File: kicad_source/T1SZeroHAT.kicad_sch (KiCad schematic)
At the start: 44 parts, among them CN1 RASPI-IO, CN2 XY2500R-F-3.81-2P, CN3 SM02B-GHS-TB, CN4 SM02B-GHS-TB, SW1 SS-3235S-L3, U1 LAN8651, Y1 X1E0000210808

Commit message: connected DIOB1 directly to GND as recommended in datasheet
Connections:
- net GND: now also U1.14 (DIOB1)
- no-connect marks 28 -> 27
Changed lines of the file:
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@@
 	)
 	(no_connect
-		(at 68.58 87.63)
-	)
-	(no_connect
 		(at 87.63 182.88)
 	)
@@
 	(wire
 		(pts
+			(xy 66.04 87.63) (xy 66.04 90.17)
+		)
+		(stroke
+			(width 0)
+			(type default)
+		)
+	)
+	(wire
+		(pts
 			(xy 111.76 64.77) (xy 121.92 64.77)
 		)
@@
 		)
 	)
+	(wire
+		(pts
+			(xy 68.58 87.63) (xy 66.04 87.63)
+		)
+		(stroke
+			(width 0)
+			(type default)
+		)
+	)
 	(text "find the full project documentation at https://github.com/generationmake/T1SZeroHAT"
 		(exclude_from_sim no)
@@
 					(unit 1)
 				)
+			)
+		)
+	)
+	(symbol
+		(lib_id "power:GND")
+		(at 66.04 90.17 0)
+		(unit 1)
+		(exclude_from_sim no)
+		(in_bom yes)
+		(on_board yes)
+		(dnp no)
+		(property "Reference" "#PWR015"
+			(at 66.04 96.52 0)
+			(effects
+				(font
+					(size 1.27 1.27)
+				)
+				(hide yes)
+			)
+		)
+		(property "Value" "GND"
+			(at 66.167 94.5642 0)
+			(effects
+				(font
+					(size 1.27 1.27)
+				)
+			)
+		)
+		(property "Footprint" ""
+			(at 66.04 90.17 0)
+			(effects
+				(font
+					(size 1.27 1.27)
+				)
+			)
+		)
+		(property "Datasheet" ""
+			(at 66.04 90.17 0)
+			(effects
+				(font
+					(size 1.27 1.27)
+				)
+			)
+		)
+		(property "Description" ""
+			(at 66.04 90.17 0)
+			(effects
+				(font
+					(size 1.27 1.27)
+				)
+				(hide yes)
+			)
+		)
+		(pin "1"
+		)
+		(instances
+			(project "T1SZeroHAT"
+				(path "/7e630080-3671-4ca2-a703-07968e580250"
+					(reference "#PWR015")
+					(unit 1)
+				)

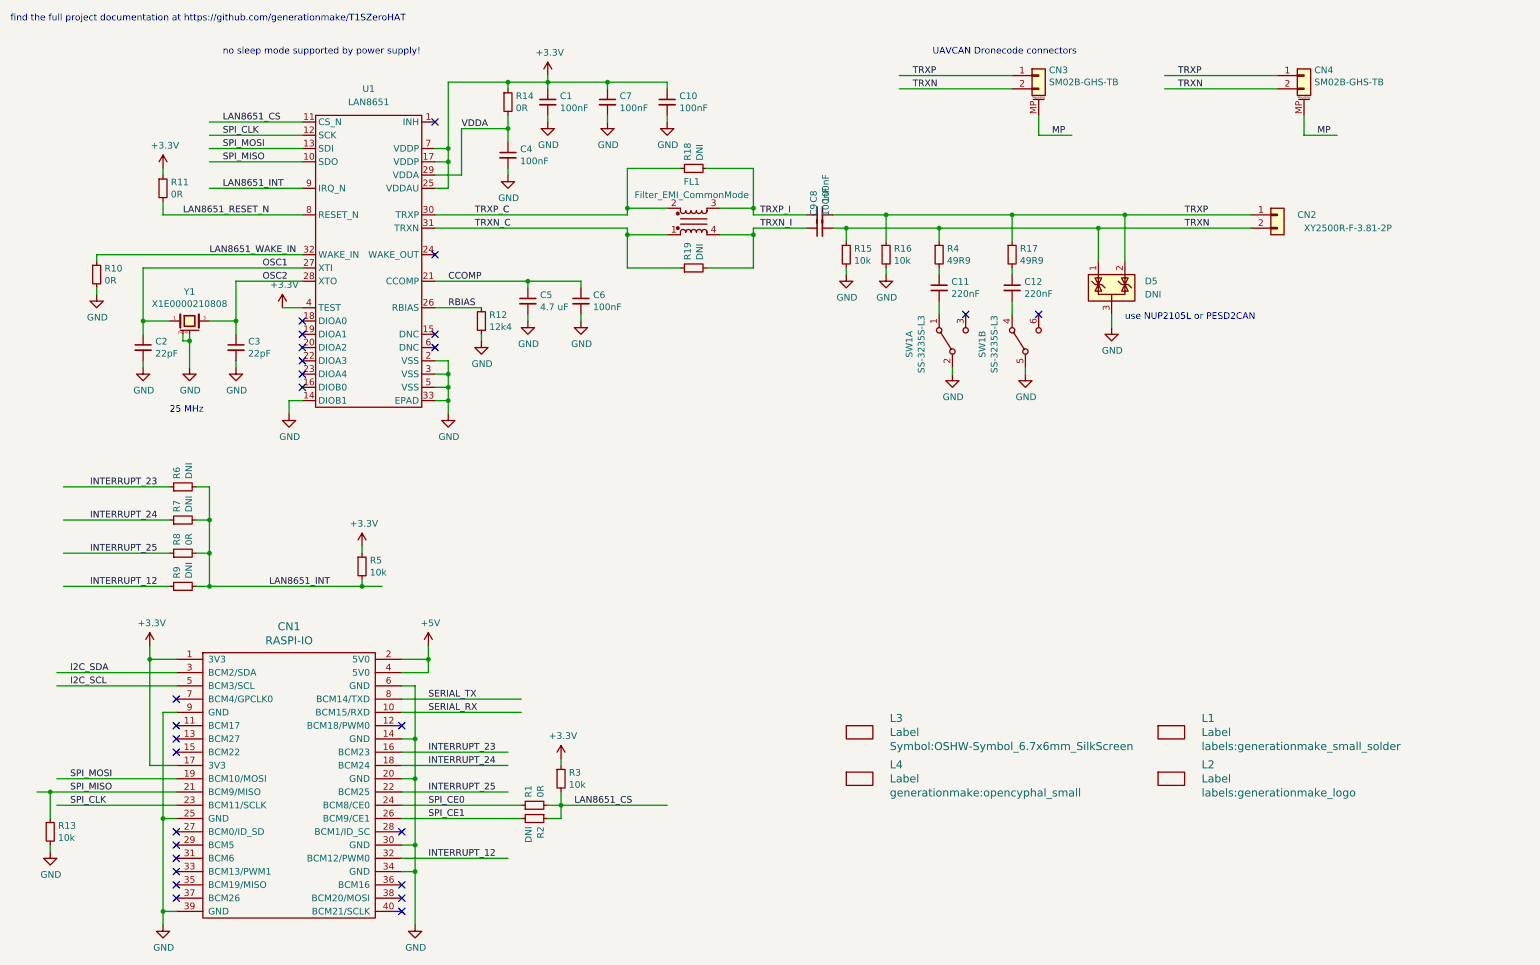
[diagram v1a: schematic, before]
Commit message: reworked power part
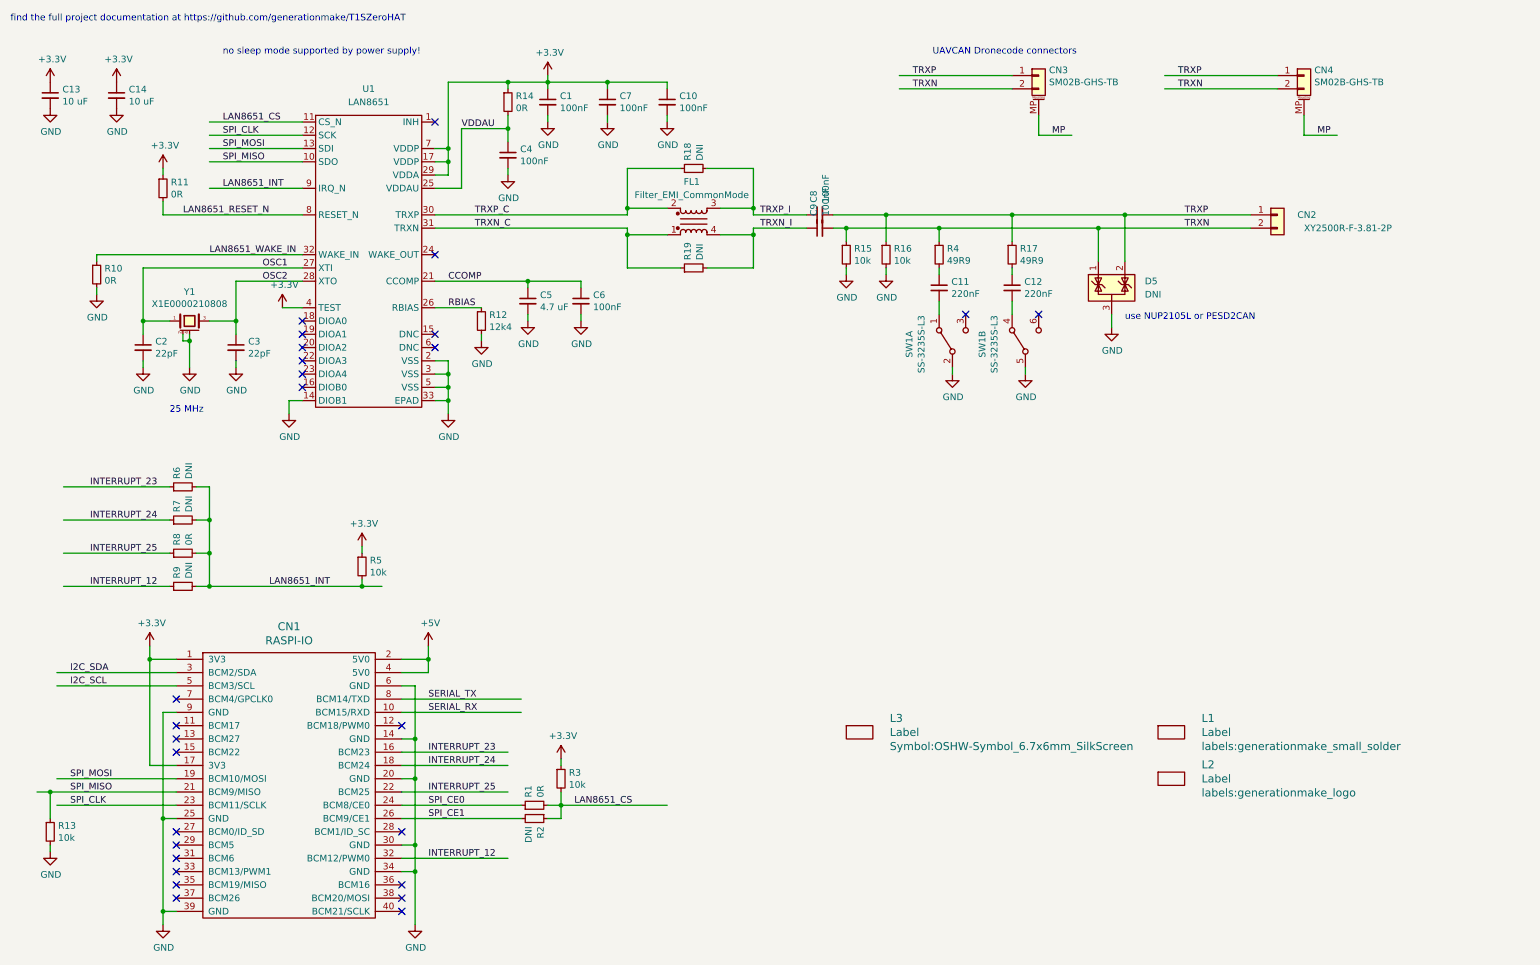
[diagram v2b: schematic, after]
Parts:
- removed L4: Label, generationmake:opencyphal_small, symbol generationmake:Label
- added C13, C14: 10 uF, Capacitor_SMD:C_0603_1608Metric, symbol Device:C_Small
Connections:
- net +3.3V: now also U1.29 (VDDA), C13.1, C14.1; no longer U1.25 (VDDAU)
- net GND: now also C13.2, C14.2
- net VDDA renamed VDDAU
- net VDDAU: now also U1.25 (VDDAU); no longer U1.29 (VDDA)

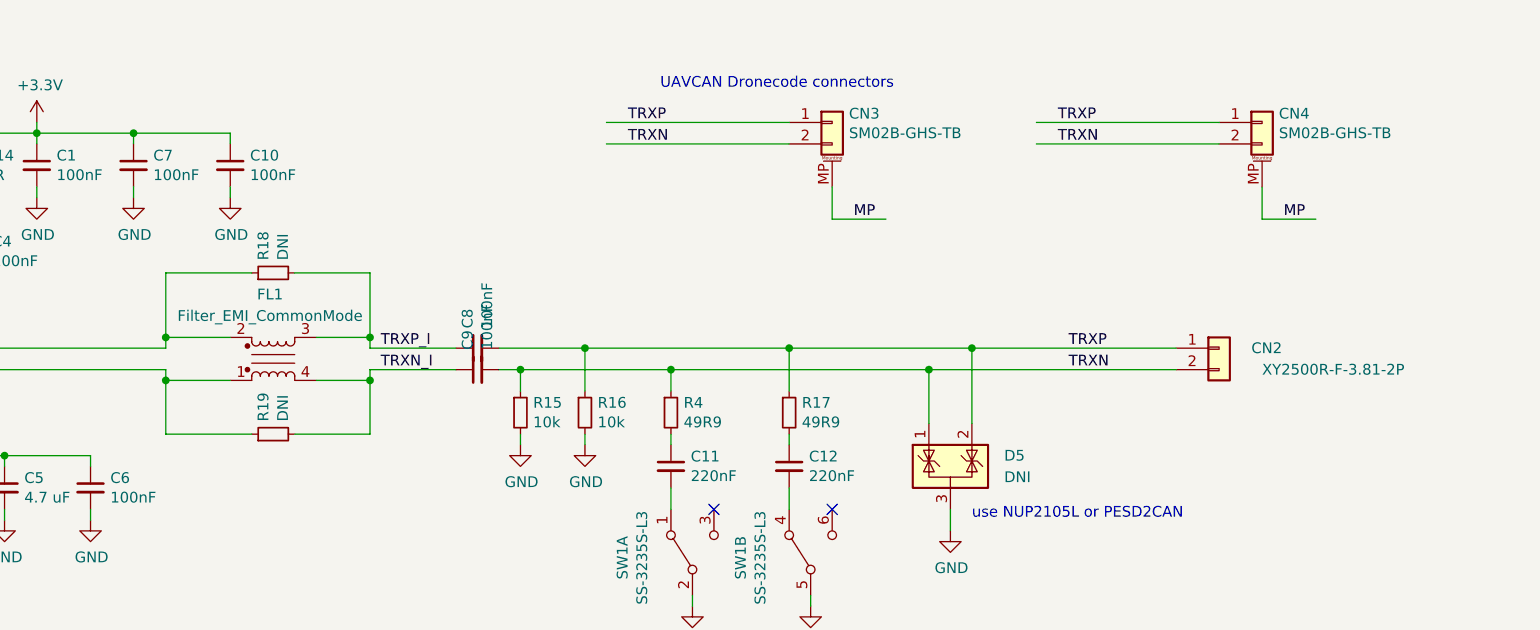
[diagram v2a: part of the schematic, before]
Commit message: corrected common mode choke and added part number
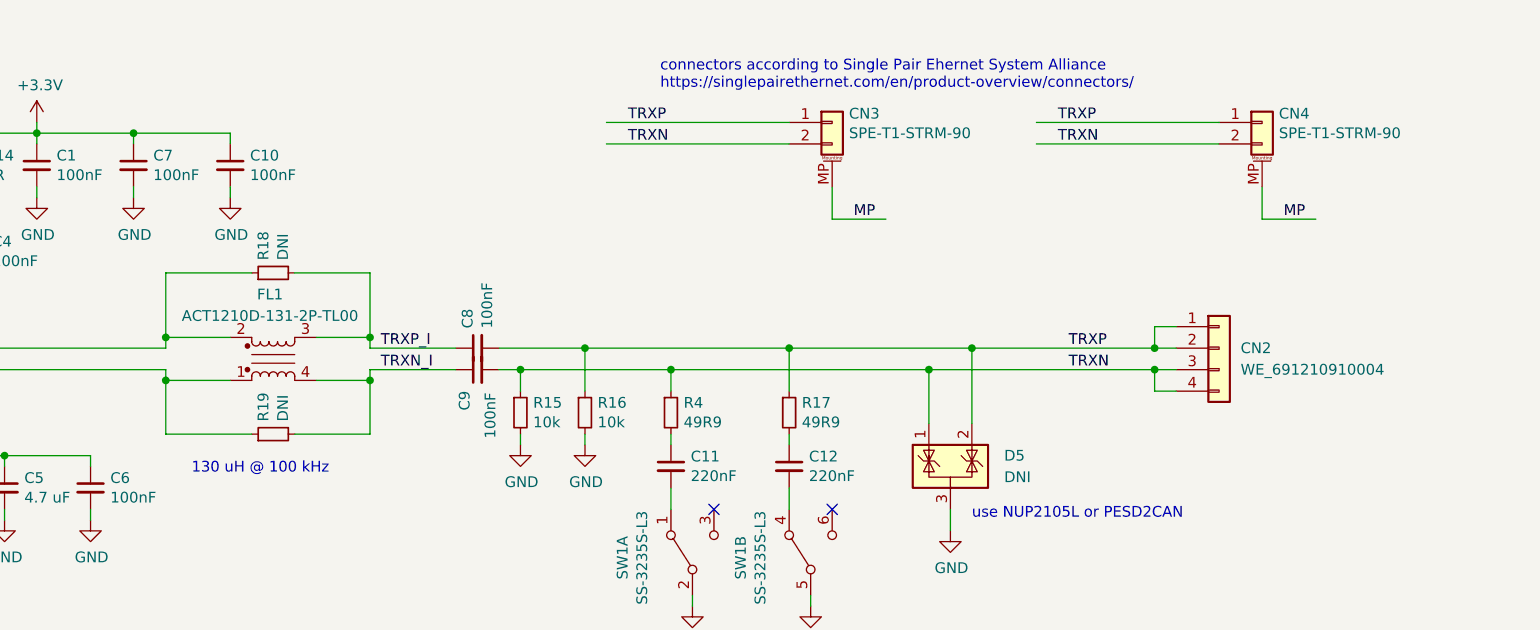
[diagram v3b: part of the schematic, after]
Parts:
- removed CN2: XY2500R-F-3.81-2P, Connector_Phoenix_MC:PhoenixContact_MC_1,5_2-G-3.81_1x02_P3.81mm_Horizontal, symbol Connector_Generic:Conn_01x02
- added CN2: WE_691210910004, generationmake:WE_691210910004, symbol Connector_Generic:Conn_01x04
- CN3, CN4: value SM02B-GHS-TB -> SPE-T1-STRM-90; footprint Connector_JST:JST_GH_SM02B-GHS-TB_1x02-1MP_P1.25mm_Horizontal -> generationmake:SPE-T1-STRM-90
- FL1: value Filter_EMI_CommonMode -> ACT1210D-131-2P-TL00; footprint Filter:Filter_Bourns_SRF0905_6.0x9.2mm -> generationmake:TDK_ACT1210D
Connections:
- net TRXN: now also CN2.3 (Pin_3), CN2.4 (Pin_4)
- net TRXP: now also CN2.1 (Pin_1), CN2.2 (Pin_2)
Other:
- note added: "130 uH @ 100 kHz"
- note added: "connectors according to Single Pair Ehernet System Alliance https://singlepairethernet.com/en/product-overview/connectors/"
- note removed: "UAVCAN Dronecode connectors"
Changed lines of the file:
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@@
 	)
 	(junction
+		(at 247.65 52.07)
+		(diameter 0)
+		(color 0 0 0 0)
+	)
+	(junction
 		(at 127 26.67)
 		(diameter 0)
@@
 	)
 	(junction
+		(at 247.65 54.61)
+		(diameter 0)
+		(color 0 0 0 0)
+	)
+	(junction
 		(at 38.1 72.39)
 		(diameter 0)
@@
 	(wire
 		(pts
+			(xy 247.65 52.07) (xy 250.19 52.07)
+		)
+		(stroke
+			(width 0)
+			(type default)
+		)
+	)
+	(wire
+		(pts
 			(xy 111.76 64.77) (xy 121.92 64.77)
 		)
@@
 	(wire
 		(pts
+			(xy 247.65 54.61) (xy 250.19 54.61)
+		)
+		(stroke
+			(width 0)
+			(type default)
+		)
+	)
+	(wire
+		(pts
 			(xy 110.49 167.64) (xy 87.63 167.64)
 		)
@@
 	(wire
 		(pts
-			(xy 220.98 54.61) (xy 250.19 54.61)
+			(xy 220.98 54.61) (xy 247.65 54.61)
+		)
+		(stroke
+			(width 0)
+			(type default)
+		)
+	)
+	(wire
+		(pts
+			(xy 250.19 57.15) (xy 247.65 57.15)
 		)
 		(stroke
@@
 	(wire
 		(pts
+			(xy 247.65 49.53) (xy 247.65 52.07)
+		)
+		(stroke
+			(width 0)
+			(type default)
+		)
+	)
+	(wire
+		(pts
 			(xy 148.59 50.8) (xy 154.94 50.8)
 		)
@@
 	(wire
 		(pts
+			(xy 247.65 57.15) (xy 247.65 54.61)
+		)
+		(stroke
+			(width 0)
+			(type default)
+		)
+	)
+	(wire
+		(pts
 			(xy 48.26 104.14) (xy 50.8 104.14)
 		)
@@
 	(wire
 		(pts
+			(xy 250.19 49.53) (xy 247.65 49.53)
+		)
+		(stroke
+			(width 0)
+			(type default)
+		)
+	)
+	(wire
+		(pts
 			(xy 93.98 41.91) (xy 96.52 41.91)
 		)
@@
 	(wire
 		(pts
-			(xy 226.06 52.07) (xy 250.19 52.07)
+			(xy 226.06 52.07) (xy 247.65 52.07)
 		)
 		(stroke
@@
 		)
 	)
+	(text "130 uH @ 100 kHz"
+		(exclude_from_sim no)
+		(at 133.858 67.056 0)
+		(effects
+			(font
+				(size 1.27 1.27)
+			)
+			(justify left bottom)
+		)
+	)
 	(text "find the full project documentation at https://github.com/generationmake/T1SZeroHAT"
 		(exclude_from_sim no)
@@
 		)
 	)
-	(text "UAVCAN Dronecode connectors"
+	(text "connectors according to Single Pair Ehernet System Alliance\nhttps://singlepairethernet.com/en/product-overview/connectors/"
 		(exclude_from_sim no)
 		(at 189.23 21.59 0)
@@
 	)
 	(symbol
-		(lib_id "Connector_Generic:Conn_01x02")
-		(at 255.27 52.07 0)
-		(unit 1)
-		(exclude_from_sim no)
-		(in_bom yes)
-		(on_board yes)
-		(dnp no)
-		(property "Reference" "CN2"
-			(at 259.08 52.07 0)
-			(effects
-				(font
-					(size 1.27 1.27)
-				)
-				(justify left)
-			)
-		)
-		(property "Value" "XY2500R-F-3.81-2P"
-			(at 260.35 54.61 0)
-			(effects
-				(font
-					(size 1.27 1.27)
-				)
-				(justify left)
-			)
-		)
-		(property "Footprint" "Connector_Phoenix_MC:PhoenixContact_MC_1,5_2-G-3.81_1x02_P3.81mm_Horizontal"
-			(at 255.27 52.07 0)
-			(effects
-				(font
-					(size 1.27 1.27)
-				)
-				(hide yes)
-			)
-		)
-		(property "Datasheet" "~"
-			(at 255.27 52.07 0)
-			(effects
-				(font
-					(size 1.27 1.27)
-				)
-				(hide yes)
-			)
-		)
-		(property "Description" ""
-			(at 255.27 52.07 0)
-			(effects
-				(font
-					(size 1.27 1.27)
-				)
-				(hide yes)
-			)
-		)
-		(property "LCSC" ""
-			(at 255.27 52.07 0)
-			(effects
-				(font
-					(size 1.27 1.27)
-				)
-				(hide yes)
-			)
-		)
-		(pin "1"
-		)
-		(pin "2"
-		)
-		(instances
-			(project ""
-				(path "/7e630080-3671-4ca2-a703-07968e580250"
-					(reference "CN2")
-					(unit 1)
-				)
-			)
-		)
-	)
-	(symbol
 		(lib_id "Switch:SW_DPDT_x2")
 		(at 193.04 76.2 90)
@@
 			)
 		)
-		(property "Value" "SM02B-GHS-TB"
+		(property "Value" "SPE-T1-STRM-90"
 			(at 211.5312 26.67 0)
 			(effects
@@
 			)
 		)
-		(property "Footprint" "Connector_JST:JST_GH_SM02B-GHS-TB_1x02-1MP_P1.25mm_Horizontal"
+		(property "Footprint" "generationmake:SPE-T1-STRM-90"
 			(at 209.55 25.4 0)
 			(effects
@@
 			)
 		)
-		(property "Value" "SM02B-GHS-TB"
+		(property "Value" "SPE-T1-STRM-90"
 			(at 262.3312 26.67 0)
 			(effects
@@
 			)
 		)
-		(property "Footprint" "Connector_JST:JST_GH_SM02B-GHS-TB_1x02-1MP_P1.25mm_Horizontal"
+		(property "Footprint" "generationmake:SPE-T1-STRM-90"
 			(at 260.35 25.4 0)
 			(effects
@@
 		(dnp no)
 		(property "Reference" "C9"
-			(at 166.4716 52.2732 0)
+			(at 166.116 59.436 0)
 			(effects
 				(font
@@
 		)
 		(property "Value" "100nF"
-			(at 168.783 52.2732 0)
+			(at 169.164 62.738 0)
 			(effects
 				(font
@@
 	)
 	(symbol
+		(lib_id "Connector_Generic:Conn_01x04")
+		(at 255.27 52.07 0)
+		(unit 1)
+		(exclude_from_sim no)
+		(in_bom yes)
+		(on_board yes)
+		(dnp no)
+		(fields_autoplaced yes)
+		(property "Reference" "CN2"
+			(at 257.81 52.0699 0)
+			(effects
+				(font
+					(size 1.27 1.27)
+				)
+				(justify left)
+			)
+		)
+		(property "Value" "WE_691210910004"
+			(at 257.81 54.6099 0)
+			(effects
+				(font
+					(size 1.27 1.27)
+				)
+				(justify left)
+			)
+		)
+		(property "Footprint" "generationmake:WE_691210910004"
+			(at 255.27 52.07 0)
+			(effects
+				(font
+					(size 1.27 1.27)
+				)
+				(hide yes)
+			)
+		)
+		(property "Datasheet" "~"
+			(at 255.27 52.07 0)
+			(effects
+				(font
+					(size 1.27 1.27)
+				)
+				(hide yes)
+			)
+		)
+		(property "Description" "Generic connector, single row, 01x04, script generated (kicad-library-utils/schlib/autogen/connector/)"
+			(at 255.27 52.07 0)
+			(effects
+				(font
+					(size 1.27 1.27)
+				)
+				(hide yes)
+			)
+		)
+		(pin "4"
+		)
+		(pin "2"
+		)
+		(pin "3"
+		)
+		(pin "1"
+		)
+		(instances
+			(project ""
+				(path "/7e630080-3671-4ca2-a703-07968e580250"
+					(reference "CN2")
+					(unit 1)
+				)
+			)
+		)
+	)
+	(symbol
 		(lib_id "Device:R_Small")
 		(at 29.21 63.5 0)
@@
 			)
 		)
-		(property "Value" "Filter_EMI_CommonMode"
+		(property "Value" "ACT1210D-131-2P-TL00"
 			(at 143.129 48.26 0)
 			(effects
@@
 			)
 		)
-		(property "Footprint" "Filter:Filter_Bourns_SRF0905_6.0x9.2mm"
+		(property "Footprint" "generationmake:TDK_ACT1210D"
 			(at 143.51 59.69 0)
 			(effects

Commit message: fixed some DRCs
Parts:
- CN1: footprint MODULE_compute:RASPI_ZERO_HAT_EDGE -> generationmake:RASPI_ZERO_HAT_EDGE
- L1: footprint labels:generationmake_small_solder -> generationmake:generationmake_small_solder
- L2: footprint labels:generationmake_logo -> generationmake:generationmake_logo
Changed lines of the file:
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@@
 			)
 		)
-		(property "Footprint" "MODULE_compute:RASPI_ZERO_HAT_EDGE"
+		(property "Footprint" "generationmake:RASPI_ZERO_HAT_EDGE"
 			(at 63.5 137.16 0)
 			(effects
@@
 			)
 		)
-		(property "Footprint" "labels:generationmake_small_solder"
+		(property "Footprint" "generationmake:generationmake_small_solder"
 			(at 240.7412 153.8224 0)
 			(effects
@@
 			)
 		)
-		(property "Footprint" "labels:generationmake_logo"
+		(property "Footprint" "generationmake:generationmake_logo"
 			(at 240.7412 162.7124 0)
 			(effects
